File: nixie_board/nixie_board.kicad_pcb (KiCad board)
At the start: 2 copper layers, 213 x 54 mm, 99 parts, among them J1 Conn_01x10_Pin, Q1 MMBTA42, Q10 MMBTA42, Q11 MMBTA42, Q12 MMBTA92, Q13 MMBTA42, Q14 MMBTA92, Q15 MMBTA42, Q16 MMBTA92, Q17 MMBTA42, Q18 MMBTA92, Q19 MMBTA42, Q2 MMBTA42, Q20 MMBTA92, Q21 MMBTA42, Q22 MMBTA92, Q23 MMBTA42, Q24 MMBTA92, Q25 MMBTA42, Q26 MMBTA92, Q27 MMBTA42, Q3 MMBTA42, Q4 MMBTA42, Q5 MMBTA42, Q6 MMBTA42, Q7 MMBTA42, Q8 MMBTA42, Q9 MMBTA42, U1 74HC595, U2 74HC595, U3 74HC595

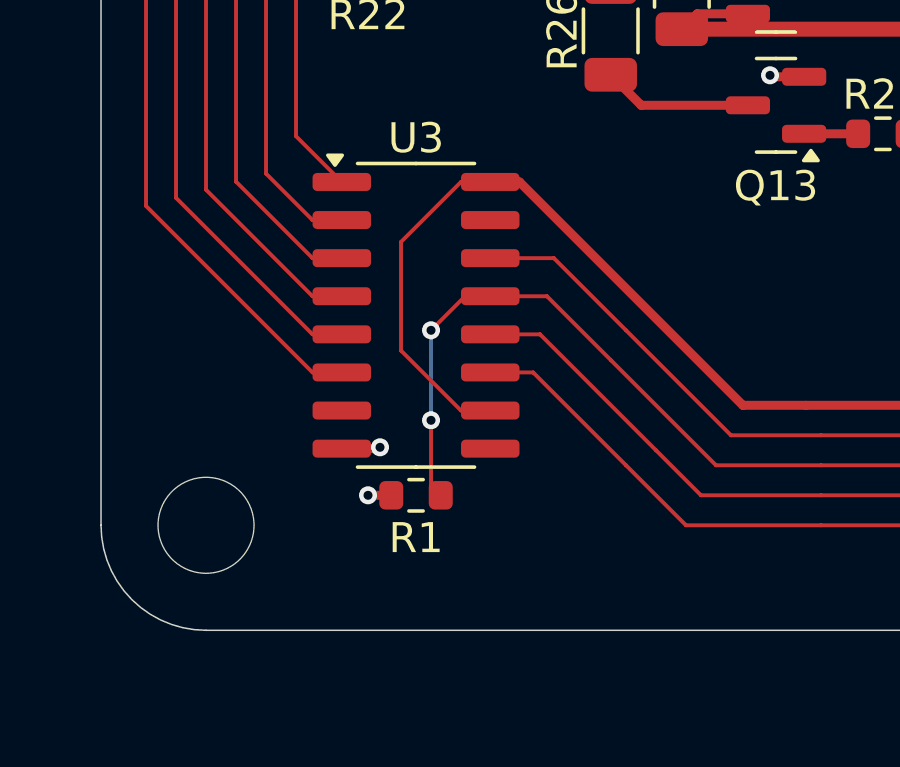
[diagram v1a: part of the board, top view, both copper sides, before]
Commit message: Added vents to case
Added vents to the underside of the case to encourage airflow.
Also fixed some stupid design mistakes on the PCBs. This is the night
before EMTH btw.
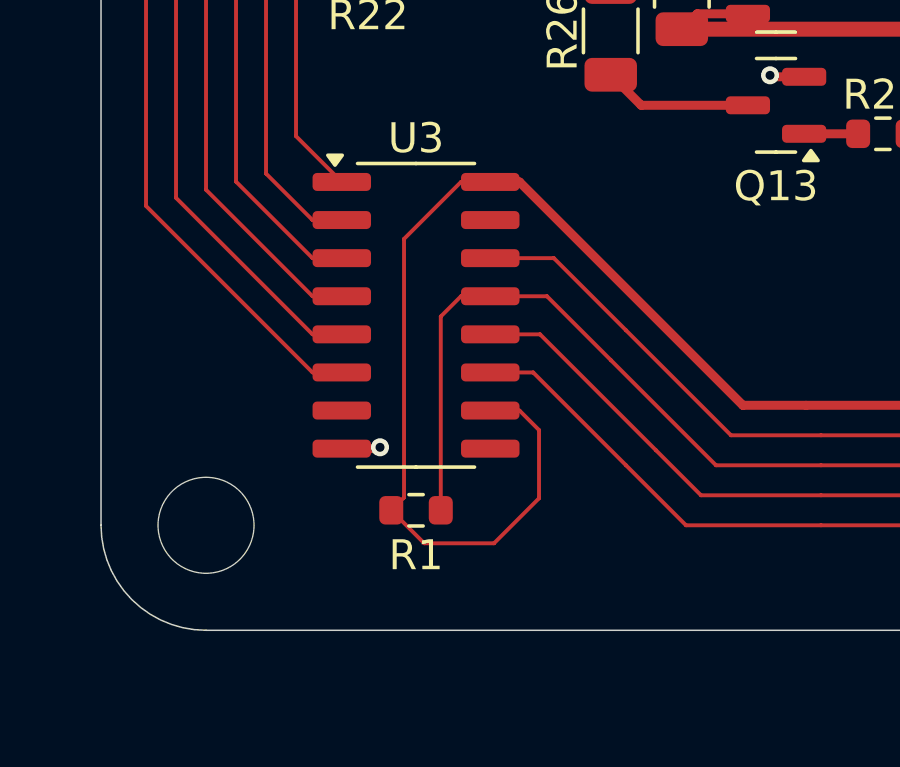
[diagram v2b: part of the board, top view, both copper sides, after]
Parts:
- moved R1 0.50 mm to (57.0, 111.5), turned to 0 degrees
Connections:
- R1 pad 1: OE -> +3V3
- R1 pad 2: GND -> OE
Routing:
- net +3V3: track 242.3 -> 254.2 mm
- net GND: track 26.2 -> 25.5 mm, vias 23 -> 22
- net OE: track 217.3 -> 217.6 mm, vias 5 -> 3
